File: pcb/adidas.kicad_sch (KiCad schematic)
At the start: 31 parts, among them J1 ISP Header, J7 Battery, J9 Shitty Add-on, U1 MPU-6050, U2 ATTINY841-SSU

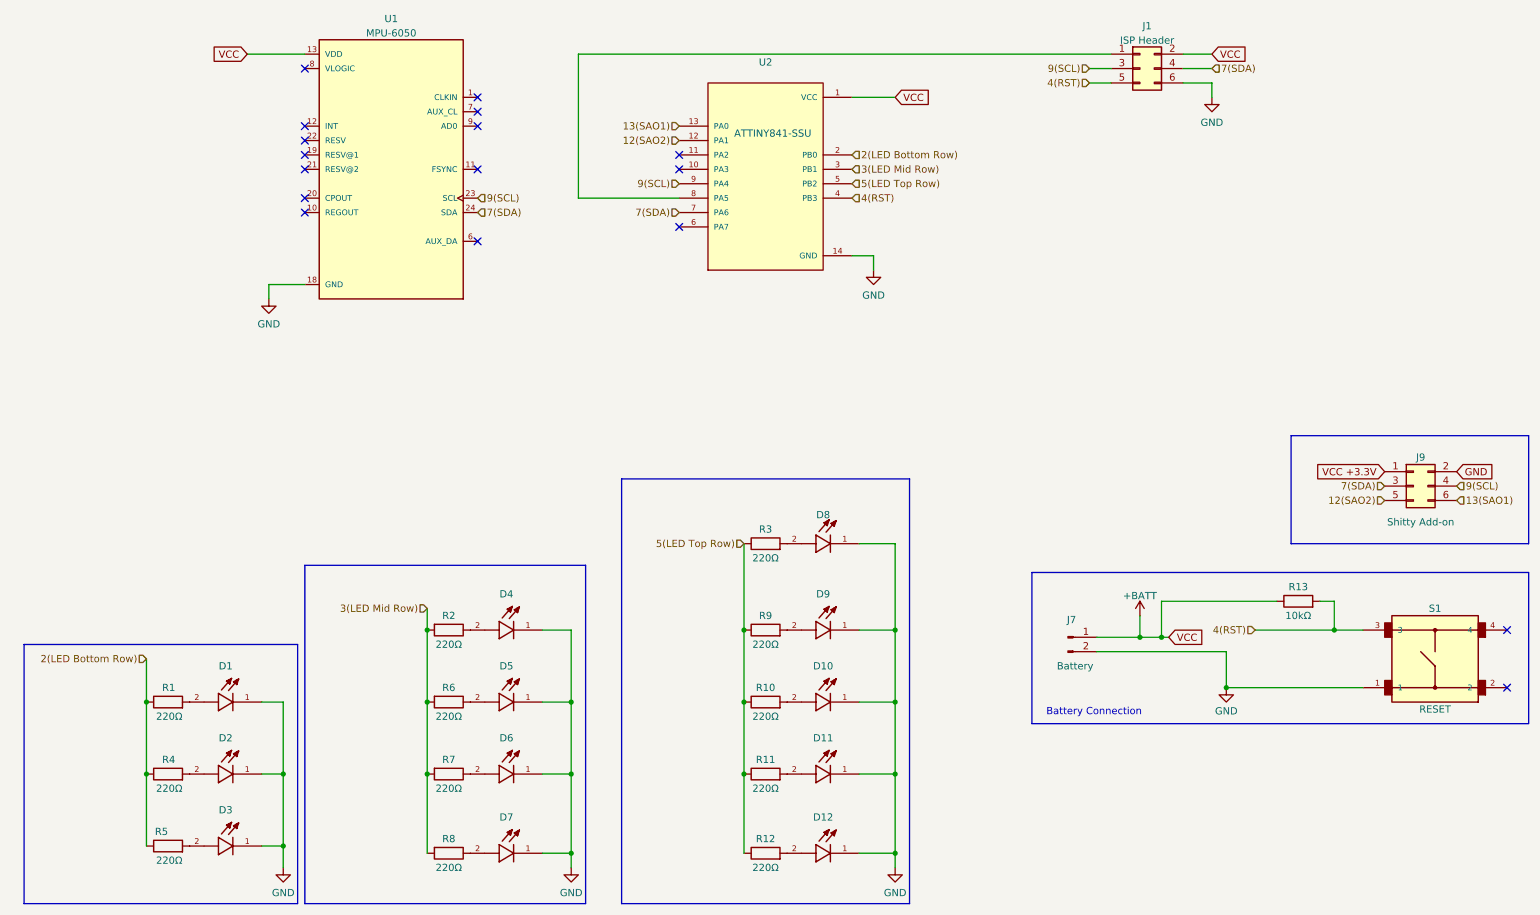
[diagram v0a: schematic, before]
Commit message: make some changes from PCBway feedback v0.3 (#27)
* make some changes from PCBway feedback v0.3

* tune actions

* add mouser and digikey part numbers

* run ERC checks

* run ERC checks
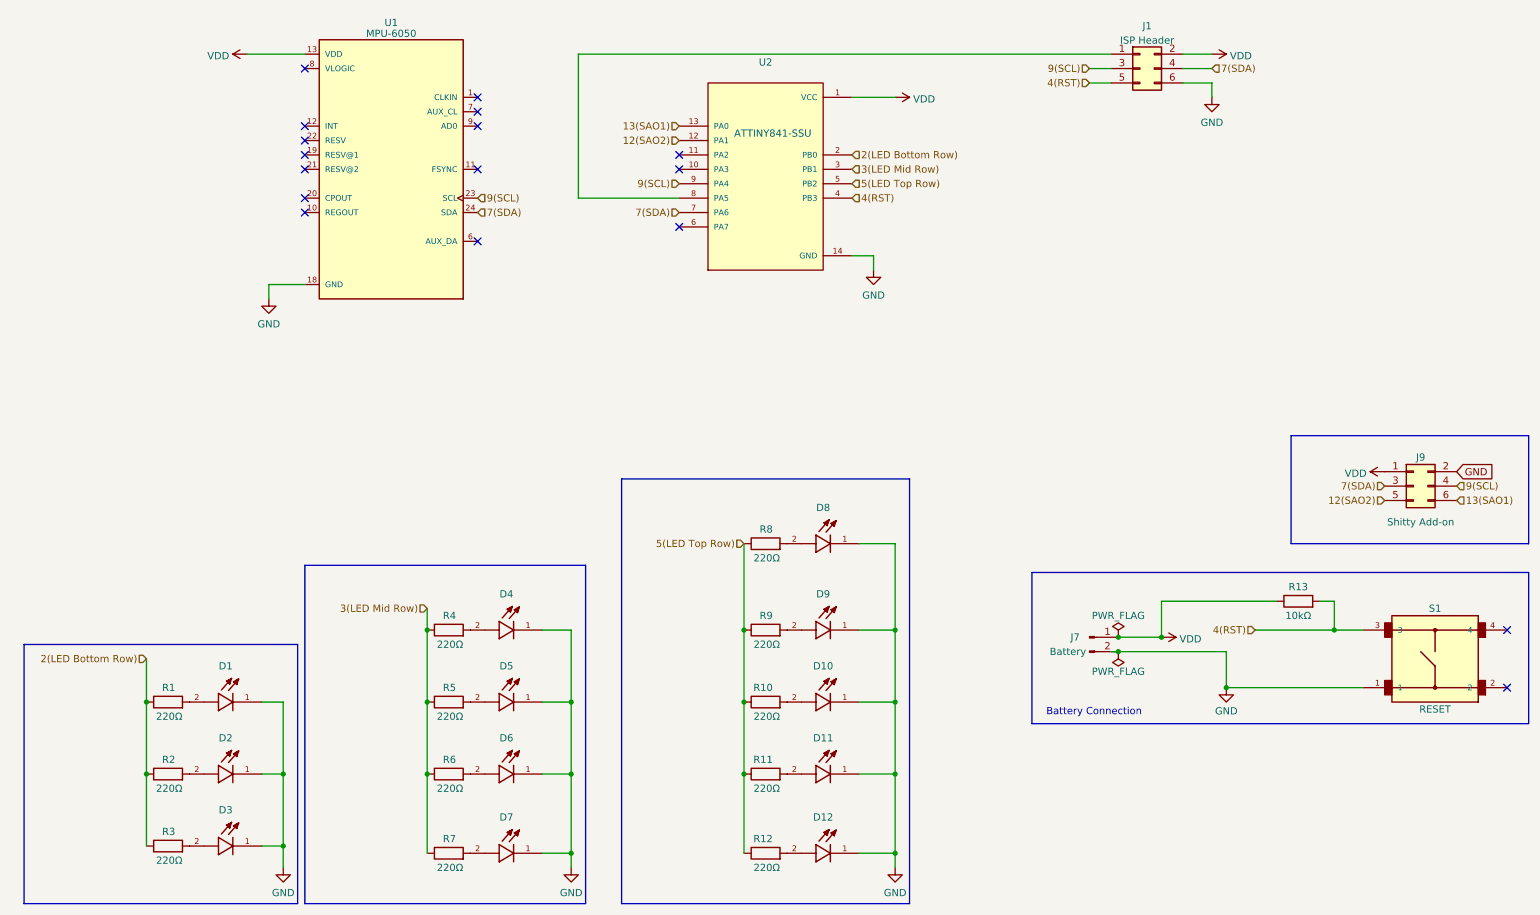
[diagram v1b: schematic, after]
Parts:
- D1, D10, D12, D2, D3, D4, D5, D6, D7, D8, D9: value LHN974 -> CTL1206FWH1T; footprint LED_SMD:LED_0805_2012Metric -> LED_SMD:LED_1206_3216Metric; Color (none) -> White; Digi-Key Part Number (none) -> 2679-CTL1206FWH1TTR-ND; MANUFACTURER Valcon -> Venkel; MAXIMUM_PACKAGE_HEIGHT 0.8mm -> 1.2mm; PARTREV A -> (none)
- D11: value ~ -> CTL1206FWH1T; footprint LED_SMD:LED_0805_2012Metric -> LED_SMD:LED_1206_3216Metric; Color (none) -> White; Digi-Key Part Number (none) -> 2679-CTL1206FWH1TTR-ND; MANUFACTURER Valcon -> Venkel; MAXIMUM_PACKAGE_HEIGHT 0.8mm -> 1.2mm; PARTREV A -> (none)
- R1: Digikey (none) -> https://www.digikey.com/en/products/detail/yageo/RC1206JR-0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; Manufacturer (none) -> YAGEO; Manufacturer Product Number (none) -> RC1206JR-07220RL
- R10, R11, R12, R2, R3, R4, R5, R6, R7, R8, R9: Digikey (none) -> https://www.digikey.com/en/products/detail/yageo/RC1206JR-0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; Manufacturer (none) -> YAGEO; Part (none) -> RC1206JR-07220RL
- R13: Digi-Key Part Number (none) -> 311-10KERCT-ND; Manufacturer (none) -> YAGEO; Manufacturer Product Number (none) -> RC1206JR-0710KL
- S1: Digi-Key Part Number (none) -> SW400-ND; MANUFACTURER Omron -> (none); Manufacturer (none) -> Omron Electronics Inc-EMC Div; now left out of the parts list
- U1: footprint DEAD10C5:QFN50P400X400X95-24N -> QFN50P400X400X95-24N; symbol MPU-6050:MPU-6050 -> dead10c5:MPU-6050; Manufacturer (none) -> TDK; Manufacturer Product Number (none) -> MPU-6050; Mouser Part  (none) -> 410-MPU-6050
- U2: footprint DEAD10C5:SOIC127P599X175-14N -> SOIC127P599X175-14N; symbol ATTINY841-SSU:ATTINY841-SSU -> dead10c5:ATTINY841-SSU; Manufacturer (none) -> Microchip; Mouser Part (none) -> 556-ATTINY841-SSU; PACKAGE_TYPE (none) -> SOIC-14
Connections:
- net VCC +3.3V is gone; now on net VDD: J9.1 (Pin_1)
- net 2(LED Bottom Row): now also R2.1, R3.1; no longer R4.1, R5.1
- net 3(LED Mid Row): now also R4.1, R5.1, R6.1, R7.1; no longer R2.2, R6.2, R7.2, R8.2
- net 5(LED Top Row): now also R8.1; no longer R3.1
- net at D8.2: now also R8.2; no longer R3.2
- net at D4.2: now also R4.2; no longer R2.1
- net at D6.2: now also R6.2; no longer R7.1
- net at D5.2: now also R5.2; no longer R6.1
- net at D3.2: now also R3.2; no longer R5.2
- net at D2.2: now also R2.2; no longer R4.2
- net at D7.2: now also R7.2; no longer R8.1
- net +BATT renamed VDD
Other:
- moved on the sheet: J7

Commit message: update schematic
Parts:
- U1: footprint QFN50P400X400X95-24N -> DEAD10C5:QFN50P400X400X95-24N
- U2: footprint SOIC127P599X175-14N -> DEAD10C5:SOIC127P599X175-14N
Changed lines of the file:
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@@
-(kicad_sch (version 20230121) (generator eeschema)
+(kicad_sch (version 20230221) (generator eeschema)
   (paper "A4")
   (title_block
@@
       (effects (font (size 1.27 1.27)))
     )
-    (property "Footprint" "SOIC127P599X175-14N" (at 146.05 66.04 0)
+    (property "Footprint" "DEAD10C5:SOIC127P599X175-14N" (at 146.05 66.04 0)
       (effects (font (size 1.27 1.27)) (justify left bottom) hide)
     )
@@
       (effects (font (size 1.27 1.27)))
     )
-    (property "Footprint" "QFN50P400X400X95-24N" (at 80.01 66.04 0)
-      (effects (font (size 1.27 1.27)) (justify left bottom) hide)
-    )
+    (property "Footprint" "DEAD10C5:QFN50P400X400X95-24N" (at 80.01 66.04 0)
+      (effects (font (size 1.27 1.27)) (justify left bottom) hide)
+    )

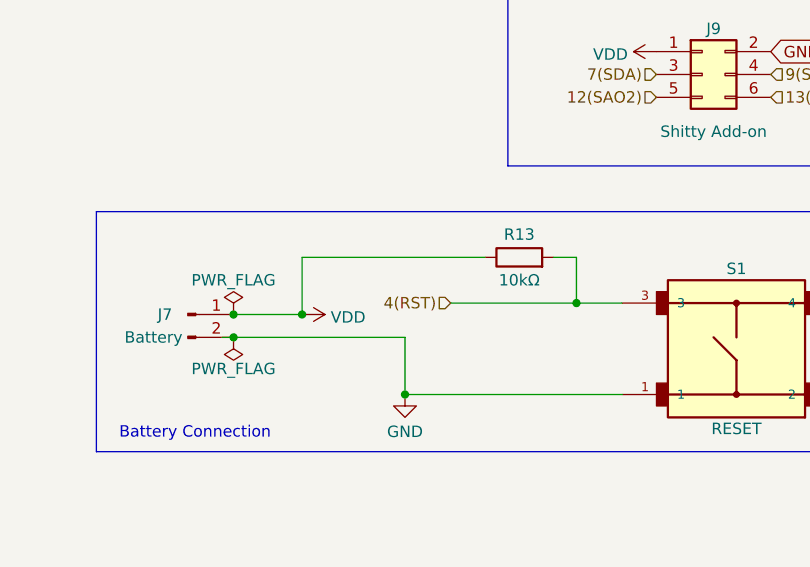
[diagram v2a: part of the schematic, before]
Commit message: update schematic
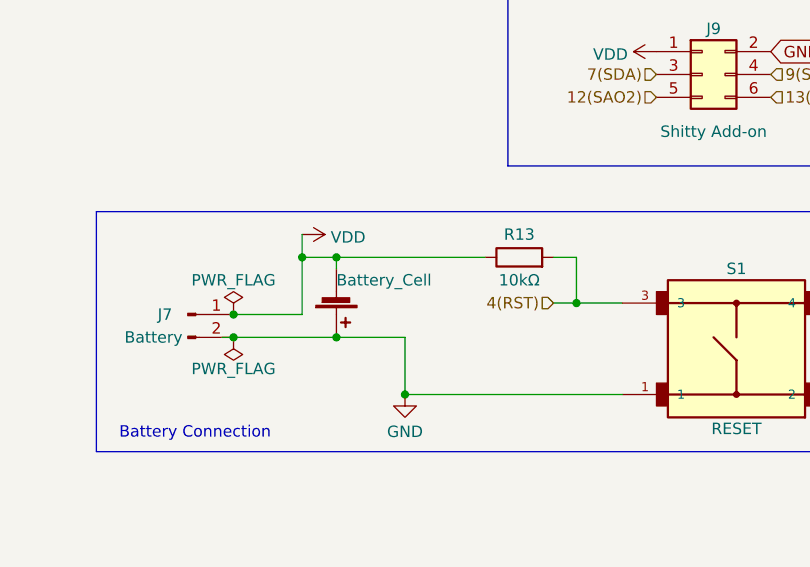
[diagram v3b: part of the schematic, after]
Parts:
- added BT1: Battery_Cell, DEAD10C5:BatteryHolder_Keystone_3002_1x2032, symbol Device:Battery_Cell
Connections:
- net GND: now also BT1.1 (+)
- net VDD: now also BT1.2 (-)
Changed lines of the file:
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@@
     (comment 1 "Русский хардбасс")
   )
+  (junction (at 219.71 151.13) (diameter 0) (color 0 0 0 0)
+  )
   (junction (at 208.28 151.13) (diameter 0) (color 0 0 0 0)
   )
@@
   (junction (at 36.83 160.02) (diameter 0) (color 0 0 0 0)
   )
+  (junction (at 215.9 142.24) (diameter 0) (color 0 0 0 0)
+  )
   (junction (at 168.91 186.69) (diameter 0) (color 0 0 0 0)
   )
-  (junction (at 215.9 148.59) (diameter 0) (color 0 0 0 0)
-  )
   (junction (at 111.76 186.69) (diameter 0) (color 0 0 0 0)
   )
@@
   )
   (junction (at 36.83 172.72) (diameter 0) (color 0 0 0 0)
+  )
+  (junction (at 219.71 142.24) (diameter 0) (color 0 0 0 0)
   )
   (junction (at 86.36 160.02) (diameter 0) (color 0 0 0 0)
@@
     (stroke (width 0) (type default))
   )
+  (wire (pts (xy 219.71 151.13) (xy 227.33 151.13))
+    (stroke (width 0) (type default))
+  )
   (wire (pts (xy 113.03 71.12) (xy 113.03 45.72))
     (stroke (width 0) (type default))
@@
     (stroke (width 0) (type default))
   )
+  (wire (pts (xy 219.71 142.24) (xy 236.22 142.24))
+    (stroke (width 0) (type default))
+  )
+  (wire (pts (xy 219.71 142.24) (xy 219.71 143.51))
+    (stroke (width 0) (type default))
+  )
+  (wire (pts (xy 215.9 139.7) (xy 215.9 142.24))
+    (stroke (width 0) (type default))
+  )
   (wire (pts (xy 111.76 172.72) (xy 111.76 186.69))
     (stroke (width 0) (type default))
@@
     (stroke (width 0) (type default))
   )
-  (wire (pts (xy 215.9 142.24) (xy 236.22 142.24))
+  (wire (pts (xy 215.9 142.24) (xy 219.71 142.24))
     (stroke (width 0) (type default))
   )
@@
     (stroke (width 0) (type default))
   )
-  (wire (pts (xy 208.28 151.13) (xy 227.33 151.13))
+  (wire (pts (xy 208.28 151.13) (xy 219.71 151.13))
     (stroke (width 0) (type default))
   )
@@
     (stroke (width 0) (type default))
   )
-  (wire (pts (xy 232.41 147.32) (xy 246.38 147.32))
+  (wire (pts (xy 243.84 147.32) (xy 246.38 147.32))
     (stroke (width 0) (type default))
   )
@@
     (effects (font (size 1.27 1.27)) (justify right))
   )
-  (hierarchical_label "4(RST)" (shape input) (at 232.41 147.32 180) (fields_autoplaced)
+  (hierarchical_label "4(RST)" (shape input) (at 243.84 147.32 180) (fields_autoplaced)
     (effects (font (size 1.27 1.27)) (justify right))
   )
@@
     )
   )
-  (symbol (lib_id "power:VDD") (at 215.9 148.59 270) (mirror x) (unit 1)
-    (in_bom yes) (on_board yes) (dnp no)
-    (property "Reference" "#PWR01" (at 212.09 148.59 0)
-      (effects (font (size 1.27 1.27)) hide)
-    )
-    (property "Value" "VDD" (at 219.075 148.9068 90)
-      (effects (font (size 1.27 1.27)) (justify left))
-    )
-    (property "Footprint" "" (at 215.9 148.59 0)
-      (effects (font (size 1.27 1.27)) hide)
-    )
-    (property "Datasheet" "" (at 215.9 148.59 0)
+  (symbol (lib_id "power:VDD") (at 215.9 139.7 270) (mirror x) (unit 1)
+    (in_bom yes) (on_board yes) (dnp no)
+    (property "Reference" "#PWR01" (at 212.09 139.7 0)
+      (effects (font (size 1.27 1.27)) hide)
+    )
+    (property "Value" "VDD" (at 219.075 140.0168 90)
+      (effects (font (size 1.27 1.27)) (justify left))
+    )
+    (property "Footprint" "" (at 215.9 139.7 0)
+      (effects (font (size 1.27 1.27)) hide)
+    )
+    (property "Datasheet" "" (at 215.9 139.7 0)
       (effects (font (size 1.27 1.27)) hide)
     )
@@
         )
       )
+    )
+  )
+  (symbol (lib_id "Device:Battery_Cell") (at 219.71 146.05 0) (mirror x) (unit 1)
+    (in_bom yes) (on_board yes) (dnp no)
+    (property "Reference" "BT1" (at 222.631 148.7257 0)
+      (effects (font (size 1.27 1.27)) (justify left) hide)
+    )
+    (property "Value" "Battery_Cell" (at 219.71 144.78 0)
+      (effects (font (size 1.27 1.27)) (justify left))
+    )
+    (property "Footprint" "DEAD10C5:BatteryHolder_Keystone_3002_1x2032" (at 219.71 147.574 90)
+      (effects (font (size 1.27 1.27)) hide)
+    )
+    (property "Datasheet" "~" (at 219.71 147.574 90)
+      (effects (font (size 1.27 1.27)) hide)
+    )
+    (pin "1")
+    (pin "2")
+    (instances
+      (project "adidas"
+        (path "/8f89af5e-dffe-4a05-a949-99c4cebef567"
+          (reference "BT1") (unit 1)
+        )
+      )

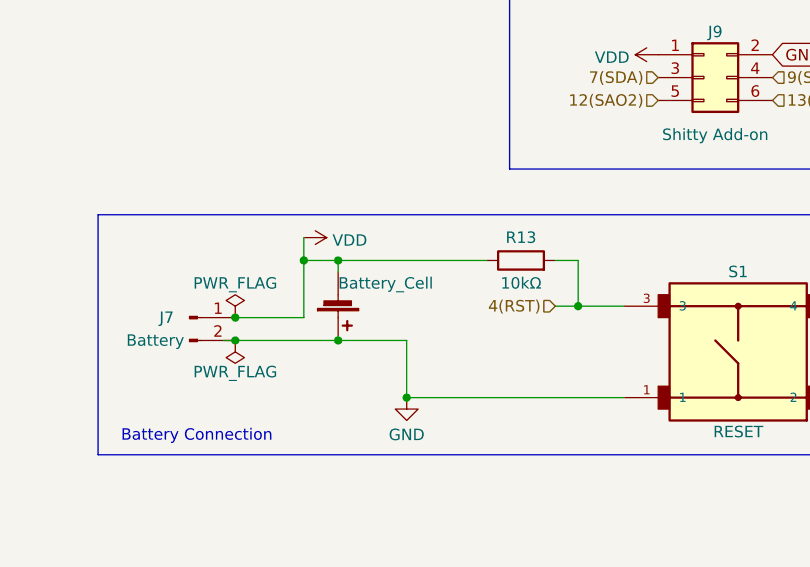
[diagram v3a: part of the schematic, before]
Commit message: update the battery clip in the BOM
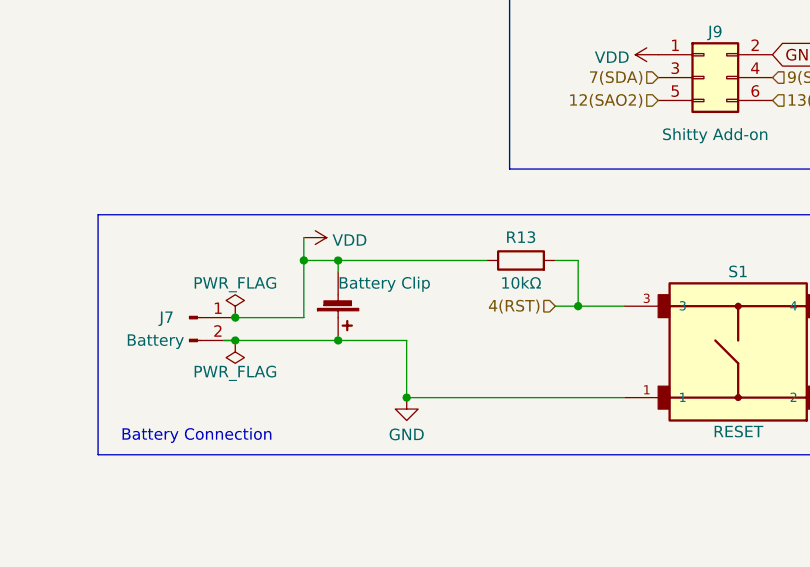
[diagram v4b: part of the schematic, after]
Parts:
- BT1: value Battery_Cell -> Battery Clip; Manufacturer (none) -> Keystone Electronics; Manufacturer Product Number (none) -> 3000TR; Mouser Part Number` (none) -> 534-3000TR; now left out of the parts list
- D10: MANUFACTURER Venkel -> (none); Manufacturer (none) -> Venkel
- U1: AVAILABILITY Good -> (none); MF TDK -> (none); PARTREV 3.4 -> (none); PRICE 5.45 USD -> (none); STANDARD IPC-7351B -> (none)
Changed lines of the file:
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@@
       (effects (font (size 1.27 1.27)) (justify bottom) hide)
     )
-    (property "MANUFACTURER" "Venkel" (at 157.48 160.02 0)
+    (property "Manufacturer" "Venkel" (at 157.48 160.02 0)
       (effects (font (size 1.27 1.27)) (justify bottom) hide)
     )
@@
   )
   (symbol (lib_id "Device:Battery_Cell") (at 219.71 146.05 0) (mirror x) (unit 1)
-    (in_bom yes) (on_board yes) (dnp no)
+    (in_bom no) (on_board yes) (dnp no)
     (property "Reference" "BT1" (at 222.631 148.7257 0)
       (effects (font (size 1.27 1.27)) (justify left) hide)
     )
-    (property "Value" "Battery_Cell" (at 219.71 144.78 0)
+    (property "Value" "Battery Clip" (at 219.71 144.78 0)
       (effects (font (size 1.27 1.27)) (justify left))
     )
@@
       (effects (font (size 1.27 1.27)) hide)
     )
-    (property "Datasheet" "~" (at 219.71 147.574 90)
+    (property "Datasheet" "https://www.mouser.com/datasheet/2/215/3000TR-742873.pdf" (at 219.71 147.574 90)
+      (effects (font (size 1.27 1.27)) hide)
+    )
+    (property "Mouser Part Number`" "534-3000TR" (at 219.71 146.05 0)
+      (effects (font (size 1.27 1.27)) hide)
+    )
+    (property "Manufacturer Product Number" "3000TR" (at 219.71 146.05 0)
+      (effects (font (size 1.27 1.27)) hide)
+    )
+    (property "Manufacturer" "Keystone Electronics" (at 219.71 146.05 0)
+      (effects (font (size 1.27 1.27)) hide)
+    )
+    (property "Description" "CR2032 Coin Cell Battery Holder" (at 219.71 146.05 0)
       (effects (font (size 1.27 1.27)) hide)
     )
@@
       (effects (font (size 1.27 1.27)) (justify left bottom) hide)
     )
-    (property "STANDARD" "IPC-7351B" (at 80.01 66.04 0)
-      (effects (font (size 1.27 1.27)) (justify left bottom) hide)
-    )
-    (property "PRICE" "5.45 USD" (at 80.01 66.04 0)
-      (effects (font (size 1.27 1.27)) (justify left bottom) hide)
-    )
     (property "DESCRIPTION" "IMU ACCEL/GYRO 3-AXIS I2C 24QFN" (at 80.01 66.04 0)
       (effects (font (size 1.27 1.27)) (justify left bottom) hide)
     )
-    (property "MF" "TDK" (at 80.01 66.04 0)
-      (effects (font (size 1.27 1.27)) (justify left bottom) hide)
-    )
-    (property "PARTREV" "3.4" (at 80.01 66.04 0)
-      (effects (font (size 1.27 1.27)) (justify left bottom) hide)
-    )
-    (property "AVAILABILITY" "Good" (at 80.01 66.04 0)
-      (effects (font (size 1.27 1.27)) (justify left bottom) hide)
-    )

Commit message: update graphics (#31)
* update graphics

* change out the LED component
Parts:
- D1, D11, D12, D2, D3, D4, D5, D6, D7, D8, D9: value CTL1206FWH1T -> SM1206NHC-IL; Color White -> (none); Digi-Key Part Number 2679-CTL1206FWH1TTR-ND -> 492-1944-1-ND; MANUFACTURER Venkel -> Bivar; MAXIMUM_PACKAGE_HEIGHT 1.2mm -> (none); Manufacturer Product Number (none) -> SM1206NHC-IL; STANDARD Manufacturer Recommendations -> (none)
- D10: value CTL1206FWH1T -> SM1206NHC-IL; Color White -> (none); Digi-Key Part Number 2679-CTL1206FWH1TTR-ND -> 492-1944-1-ND; MANUFACTURER (none) -> Bivar; MAXIMUM_PACKAGE_HEIGHT 1.2mm -> (none); Manufacturer Venkel -> (none); Manufacturer Product Number (none) -> SM1206NHC-IL; STANDARD Manufacturer Recommendations -> (none)
